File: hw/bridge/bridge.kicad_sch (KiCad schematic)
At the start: 20 parts, among them J1 USB_C_Receptacle_USB2.0_14P, J2 USB_C_Receptacle_USB2.0_14P, J3 DB9, U2 MAX485E, U3 CH340E

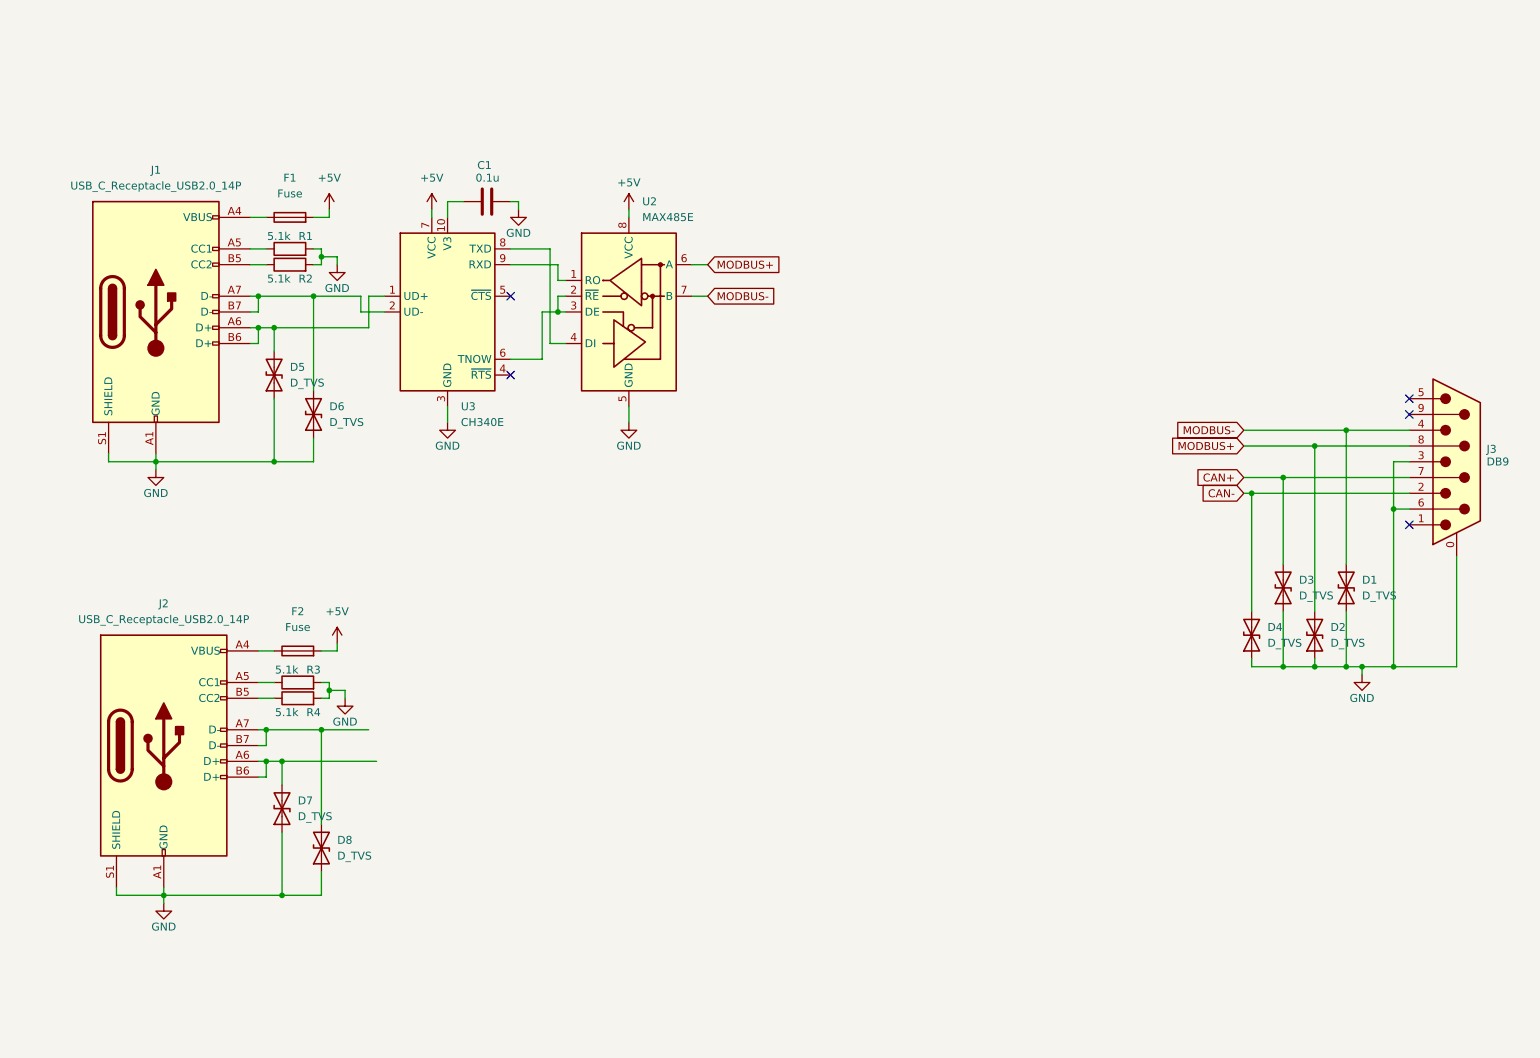
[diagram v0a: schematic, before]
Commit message: Add USB to RS485/CAN bridge sch
Signed-off-by: Mateusz Pająk <22417805+Tai-Min@users.noreply.github.com>
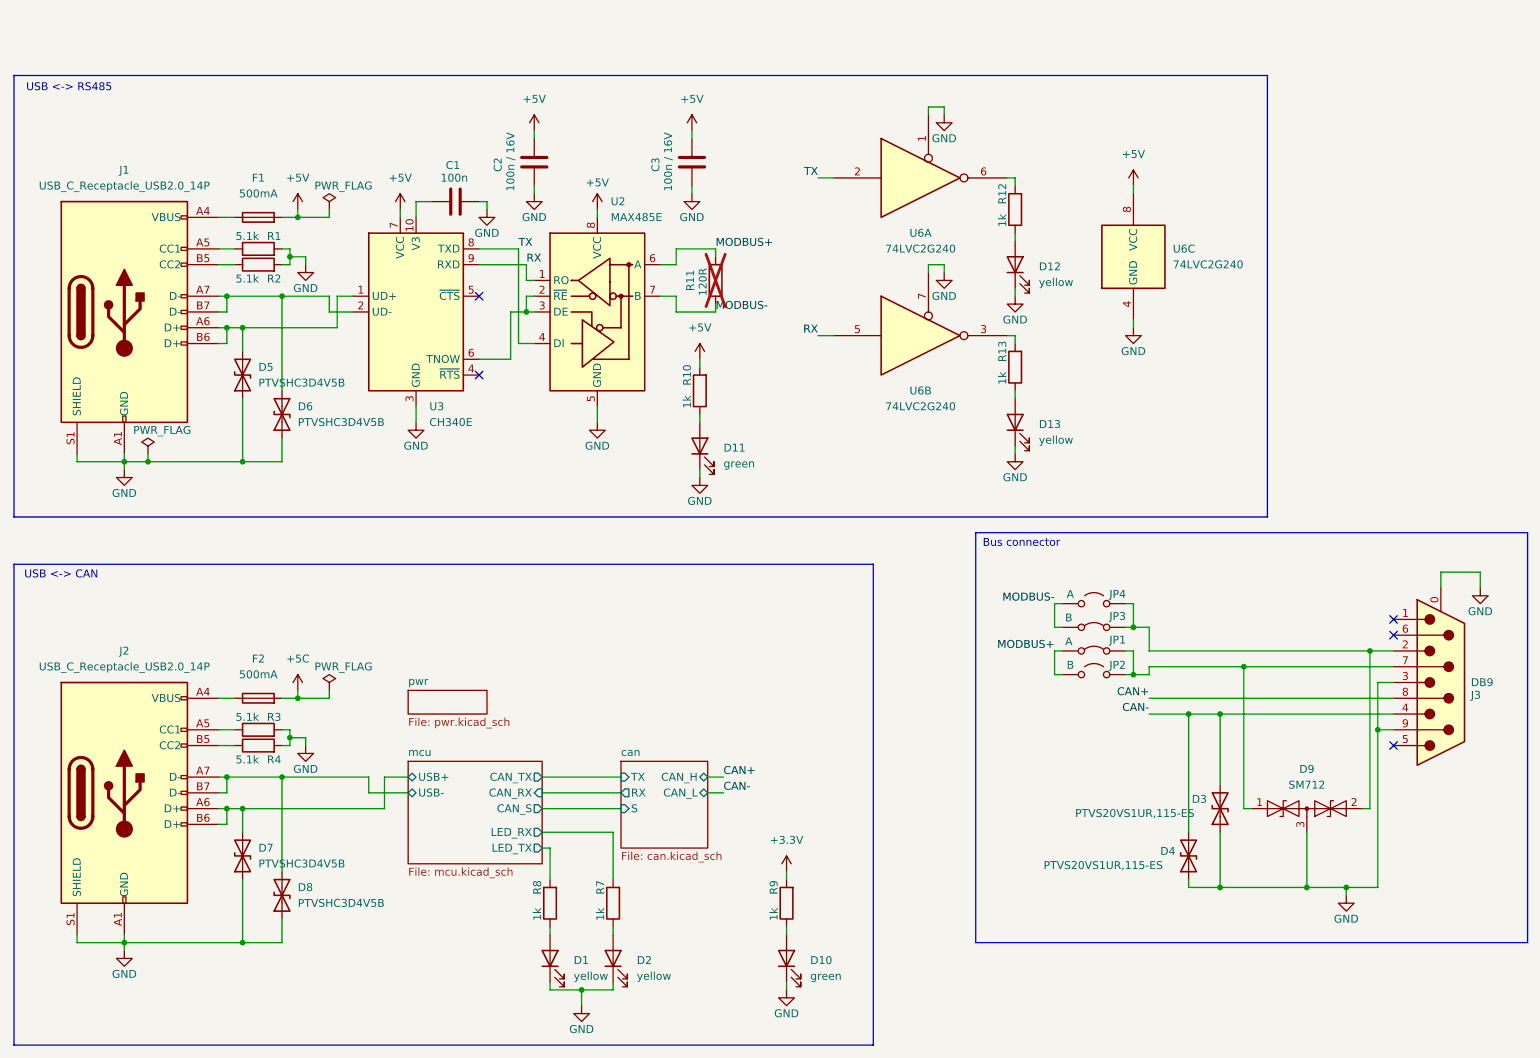
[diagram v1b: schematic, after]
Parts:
- removed D1, D2: D_TVS, symbol Device:D_TVS
- added C2, C3: 100n / 16V, symbol Device:C
- added D1, D12, D13, D2: yellow, symbol Device:LED
- added D10, D11: green, symbol Device:LED
- added D9: SM712, Package_TO_SOT_SMD:SOT-23, symbol Diode:SM712_SOT23
- added JP1: A, symbol Jumper:Jumper_2_Bridged
- added JP2: B, symbol Jumper:Jumper_2_Open
- added JP3: B, symbol Jumper:Jumper_2_Bridged
- added JP4: A, symbol Jumper:Jumper_2_Open
- added R10, R12, R13, R7, R8, R9: 1k, symbol Device:R
- added R11: 120R, symbol Device:R
- added U6: 74LVC2G240, symbol 74xGxx:74LVC2G240
- C1: value 0.1u -> 100n
- D3, D4: value D_TVS -> PTVS20VS1UR,115-ES
- D5, D6, D7, D8: value D_TVS -> PTVSHC3D4V5B
- F1, F2: value Fuse -> 500mA
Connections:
- net +5V: now also C2.2, C3.2, R10.2, U6.8 (VCC); no longer F2.2
- net CAN+: now also J3.8; no longer D3.2 (A2), J3.7
- net CAN-: now also D3.2 (A2), J3.4; no longer J3.2
- net GND: now also J3.9, C2.1, C3.1, D1.1 (K), D10.1 (K), D11.1 (K), D12.1 (K), D13.1 (K), D2.1 (K), D9.3 (common), U6.1, U6.4 (GND), U6.7; no longer J3.6
- net MODBUS+: now also JP1.1 (A), JP2.1 (A), R11.2; no longer J3.8
- net MODBUS-: now also JP3.1 (A), JP4.1 (A), R11.1; no longer J3.4
- net mcu/USB+: now reaches D7.2 (A2), J2.A6 (D+), J2.B6 (D+)
- net mcu/USB-: now reaches D8.2 (A2), J2.A7 (D-), J2.B7 (D-)
- net TX: now reaches U2.4 (DI), U3.8 (TXD)
- net TX: now also U6.2
- net RX: now reaches U2.1 (RO), U3.9 (RXD)
- net RX: now also U6.5
- new net: D9.1 (A1), J3.7, JP1.2 (B), JP2.2 (B)
- new net: D2.2 (A), R7.1
- new net: D10.2 (A), R9.1
- new net: D13.2 (A), R13.1
- new net: R13.2, U6.3
- new net: D9.2 (A2), J3.2, JP3.2 (B), JP4.2 (B)
- new net: D12.2 (A), R12.1
- new net: D11.2 (A), R10.1
- new net: D1.2 (A), R8.1
- new net: R12.2, U6.6
- new net +3.3V: R9.2
- new net +5C: F2.2
- new net mcu/LED_RX: R7.2
- new net mcu/LED_TX: R8.2
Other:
- added sheet can (can.kicad_sch)
- added sheet mcu (mcu.kicad_sch)
- added sheet pwr (pwr.kicad_sch)
- note added: "Bus connector"
- note added: "USB <-> CAN"
- note added: "USB <-> RS485"
- moved on the sheet: C1, D3, D4, D5, D6, D7, D8, F1, F2, J1, J2, J3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

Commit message: Add initial PCB to the bridge
Signed-off-by: Mateusz Pająk <22417805+Tai-Min@users.noreply.github.com>
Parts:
- C1, C2, C3: footprint (none) -> Capacitor_SMD:C_1206_3216Metric
- D1, D10, D11, D12, D13, D2: footprint (none) -> LED_SMD:LED_1206_3216Metric
- D3, D4: footprint (none) -> Diode_SMD:D_SOD-123F; now not fitted
- D5, D6, D7, D8: footprint (none) -> Diode_SMD:D_SOD-323
- D9: now not fitted
- F1, F2: footprint (none) -> Fuse:Fuse_1206_3216Metric
- J1, J2: footprint (none) -> Connector_USB:USB_C_Receptacle_Amphenol_12401610E4-2A_CircularHoles
- JP1, JP3: footprint (none) -> Jumper:SolderJumper-2_P1.3mm_Bridged2Bar_Pad1.0x1.5mm
- JP2, JP4: footprint (none) -> Jumper:SolderJumper-2_P1.3mm_Open_Pad1.0x1.5mm
- R1, R10, R11, R12, R13, R2, R3, R4, R7, R8, R9: footprint (none) -> Resistor_SMD:R_1206_3216Metric
- U6: footprint (none) -> Package_SO:TSSOP-8_3x3mm_P0.65mm
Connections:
- net CAN+: now also D3.2 (A2), J3.7; no longer J3.8
- net CAN-: now also J3.2; no longer D3.2 (A2), J3.4
- net GND: now also J3.6; no longer J3.9
- net M+: now reaches D9.1 (A1), JP1.2 (B), JP2.2 (B)
- net M+: now also J3.8; no longer J3.7
- net RS_D-: now reaches D6.2 (A2), J1.A7 (D-), J1.B7 (D-), U3.2 (UD-)
- net RS_D+: now reaches D5.2 (A2), J1.A6 (D+), J1.B6 (D+), U3.1 (UD+)
- net M-: now reaches D9.2 (A2), JP3.2 (B), JP4.2 (B)
- net M-: now also J3.4; no longer J3.2
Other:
- note added: "Bus connector is already protected"
- moved on the sheet: J3

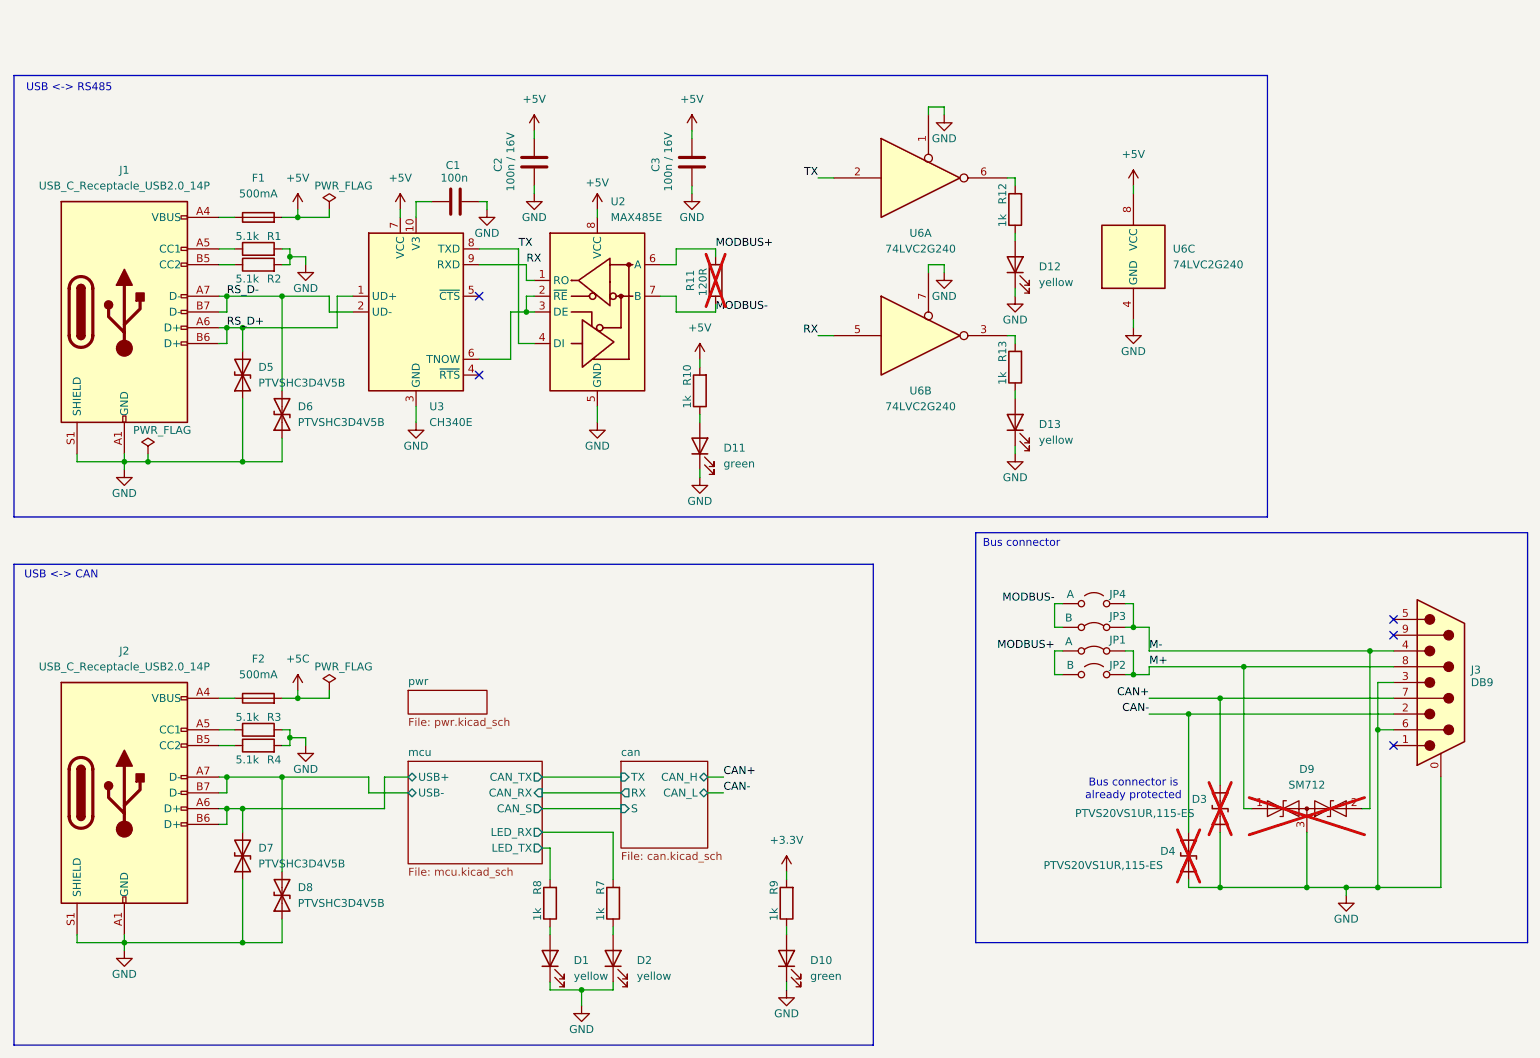
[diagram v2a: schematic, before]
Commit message: Fix jumpers
Signed-off-by: Mateusz Pająk <22417805+Tai-Min@users.noreply.github.com>
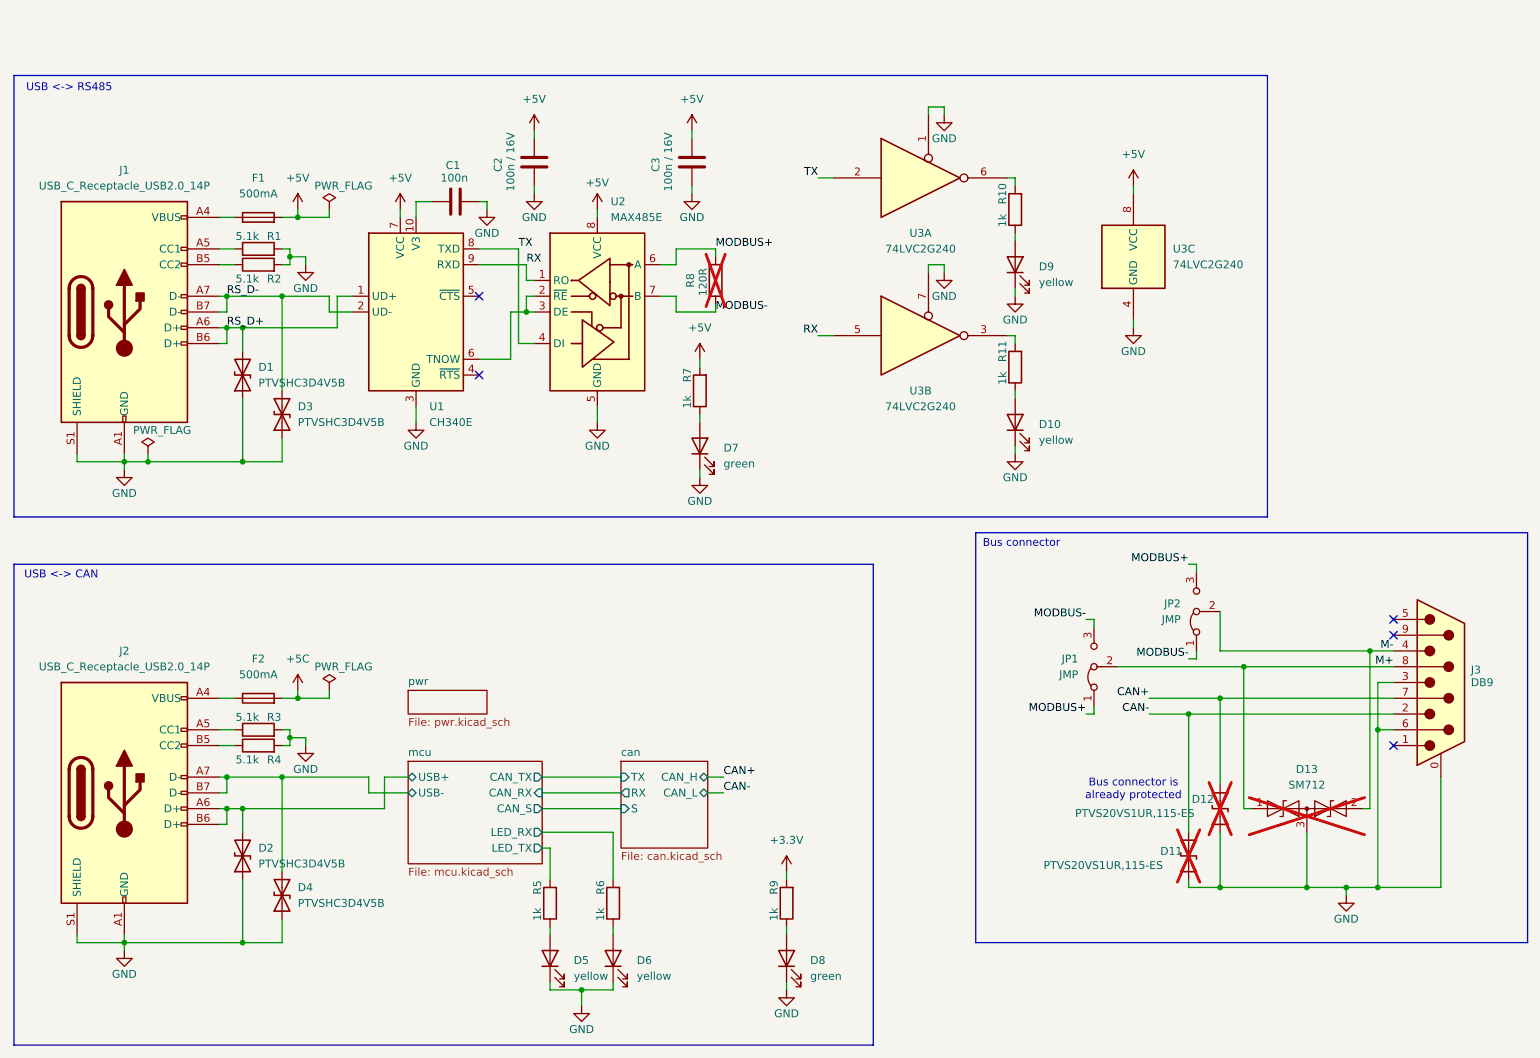
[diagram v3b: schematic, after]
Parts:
- removed JP1: A, Jumper:SolderJumper-2_P1.3mm_Bridged2Bar_Pad1.0x1.5mm, symbol Jumper:Jumper_2_Bridged
- removed JP2: B, Jumper:SolderJumper-2_P1.3mm_Open_Pad1.0x1.5mm, symbol Jumper:Jumper_2_Open
- removed JP3: B, Jumper:SolderJumper-2_P1.3mm_Bridged2Bar_Pad1.0x1.5mm, symbol Jumper:Jumper_2_Bridged
- removed JP4: A, Jumper:SolderJumper-2_P1.3mm_Open_Pad1.0x1.5mm, symbol Jumper:Jumper_2_Open
- added JP1, JP2: JMP, Jumper:SolderJumper-3_P1.3mm_Bridged2Bar12_RoundedPad1.0x1.5mm, symbol Jumper:Jumper_3_Bridged12
- renumbered D5 to D1, D13 to D10, D4 to D11, D3 to D12, D9 to D13, D7 to D2, D6 to D3, D8 to D4, D1 to D5, D2 to D6, D11 to D7, D10 to D8, D12 to D9, R12 to R10, R13 to R11, R8 to R5, R7 to R6, R10 to R7, R11 to R8, U3 to U1, U6 to U3
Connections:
- net M+: now also JP1.2 (C)
- net M-: now also JP2.2 (C)
- net MODBUS+: now also JP1.1 (A), JP2.3 (B)
- net MODBUS-: now also JP1.3 (B), JP2.1 (A)
